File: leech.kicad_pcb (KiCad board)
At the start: 2 copper layers, 17.8 x 43.2 mm, 15 parts, among them CN1 WeActBoard_noswd, U1 ICE40UP5K-SG48ITR, U2 STMPS2151STR, U3 TPS73101DBV

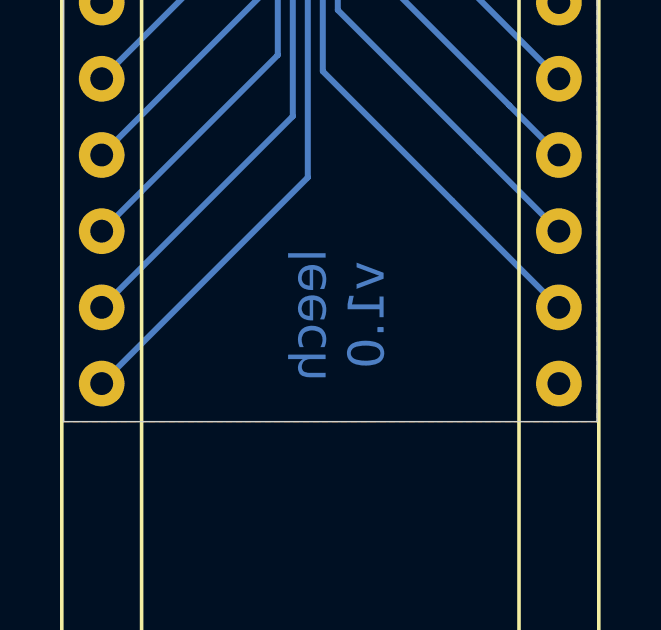
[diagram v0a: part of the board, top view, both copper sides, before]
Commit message: Update board version to 1.2, regenerate gerbers
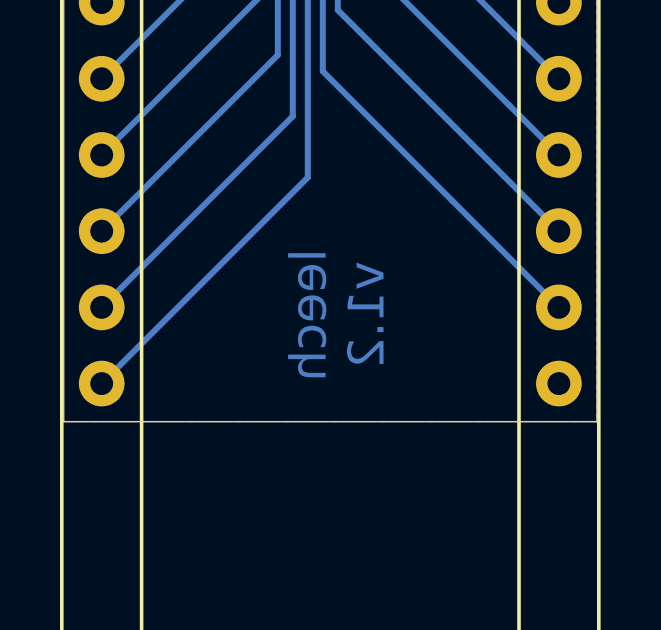
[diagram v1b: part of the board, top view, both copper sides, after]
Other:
- board text added: "leech v1.2"
- board text removed: "leech v1.0"
